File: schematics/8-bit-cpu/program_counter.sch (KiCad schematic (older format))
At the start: 6 parts

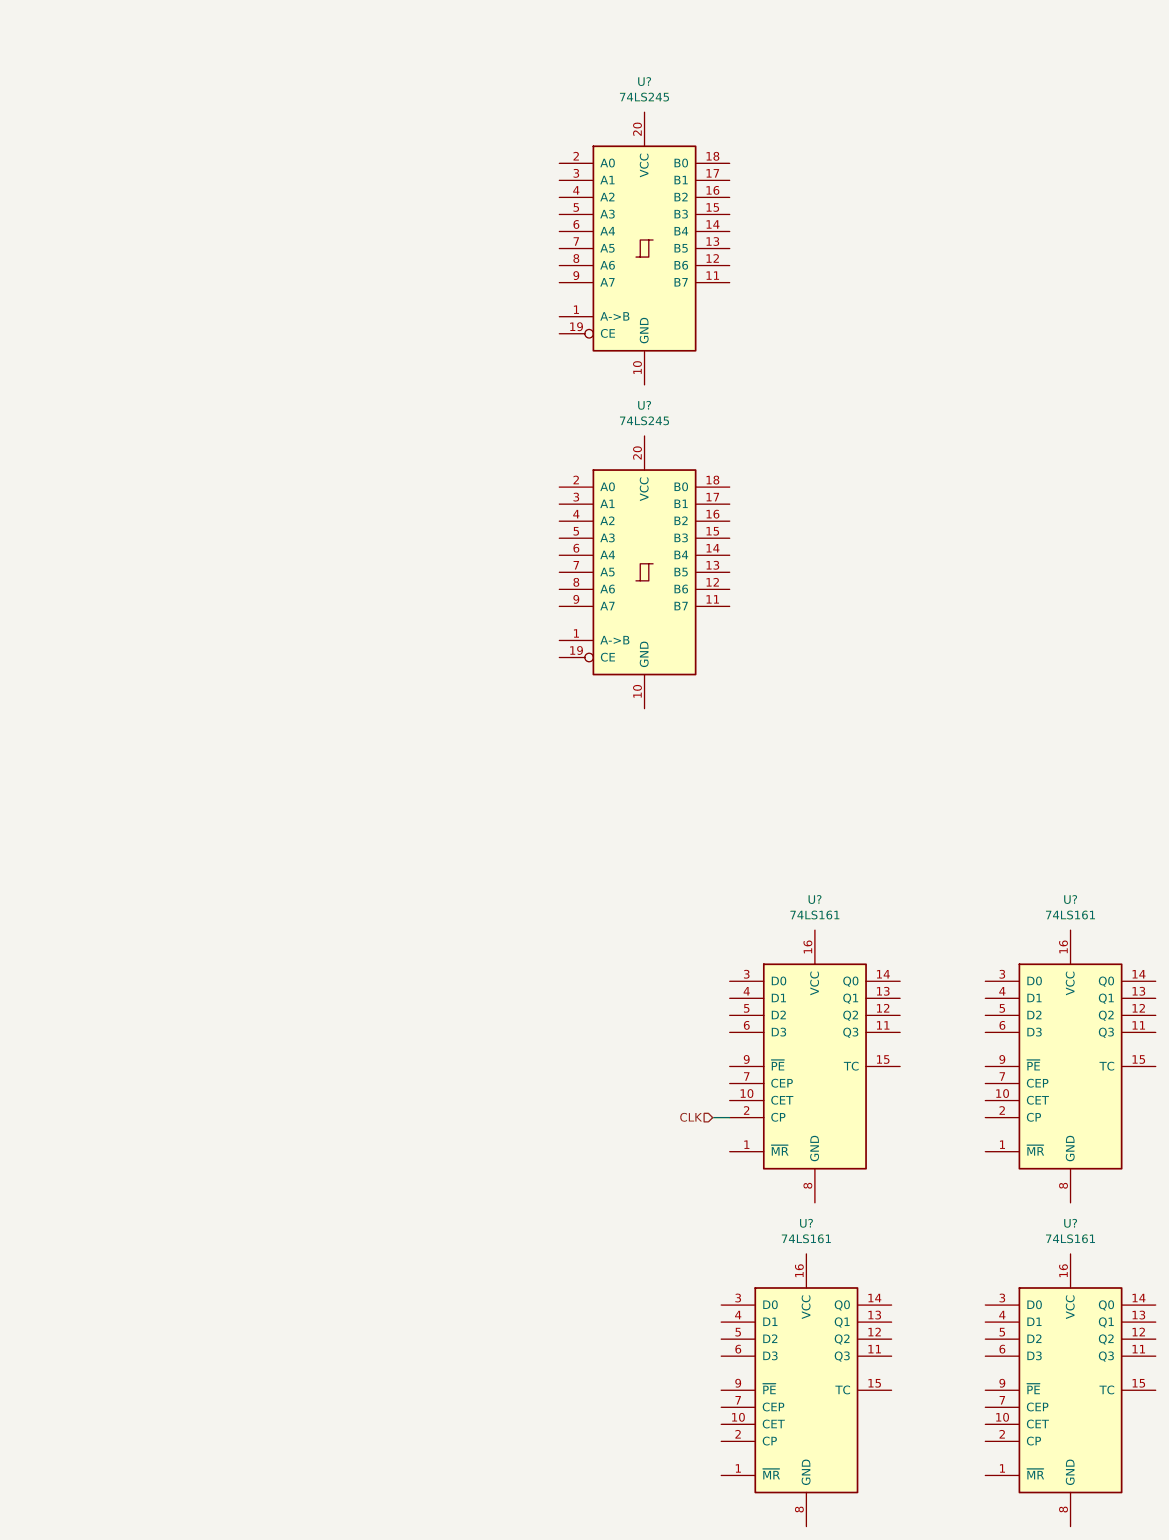
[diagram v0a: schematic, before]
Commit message: Added ALU, Accumulator and HL register schematics
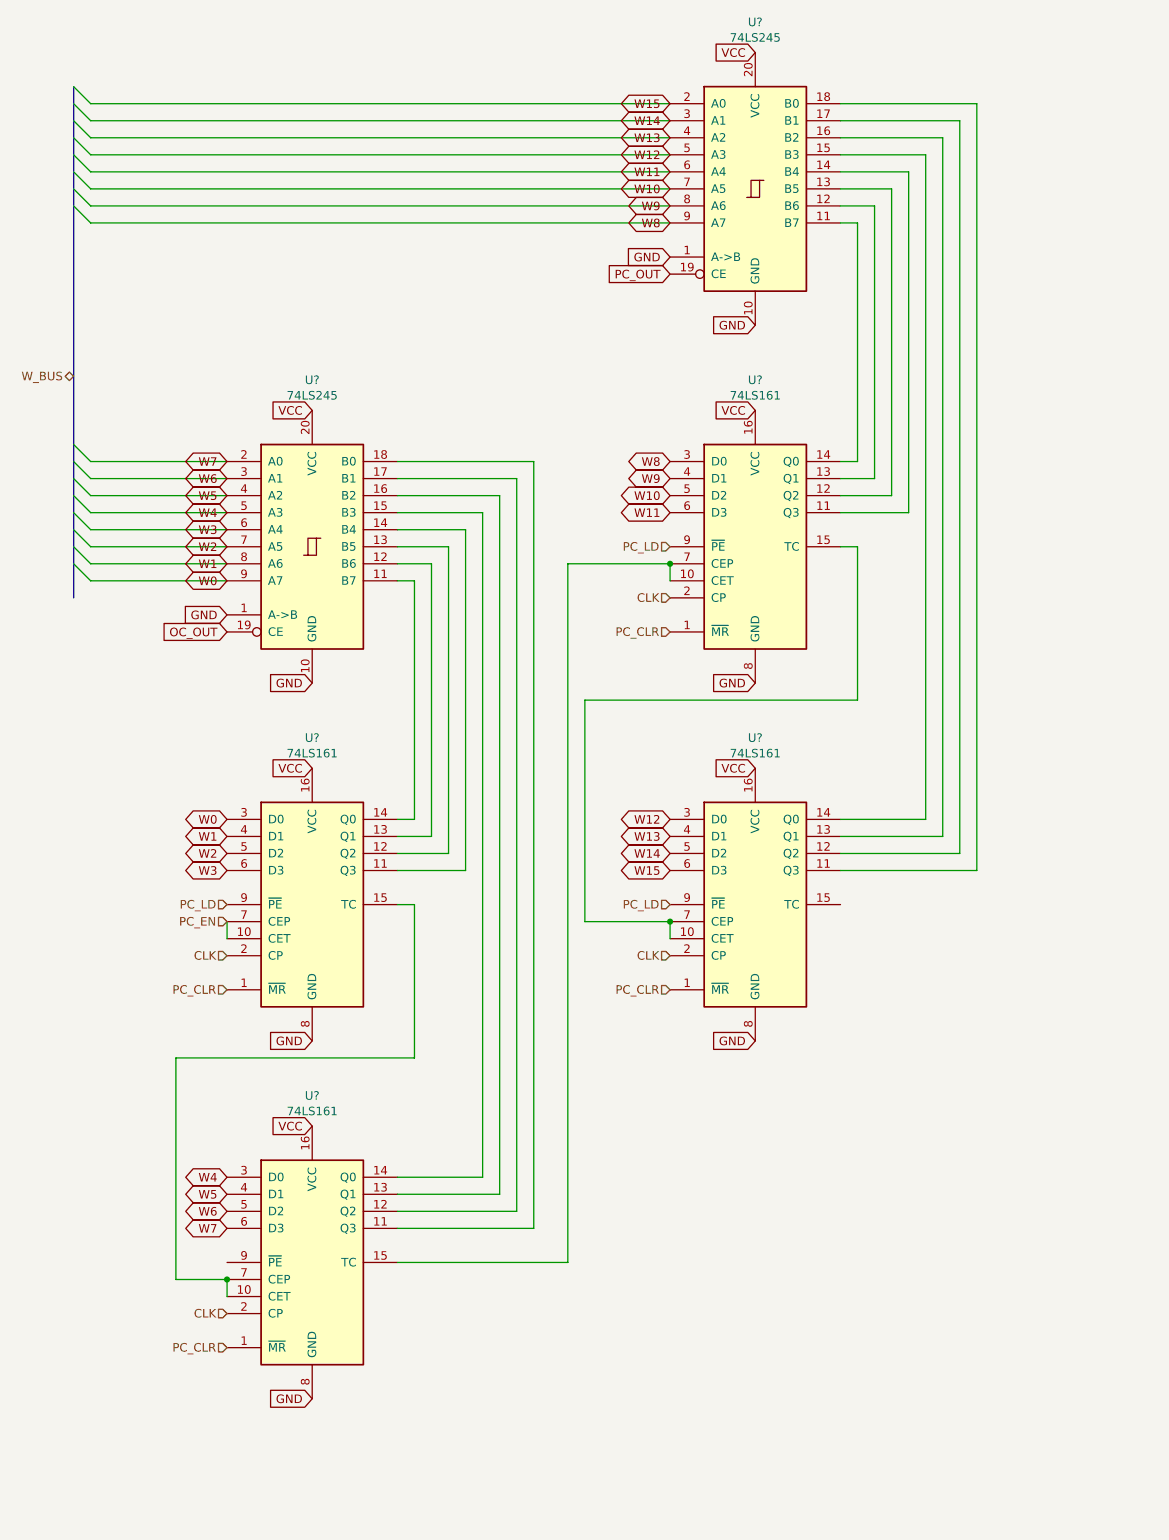
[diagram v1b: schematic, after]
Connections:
- net CLK: now also U?.2 (CP), U?.2 (CP), U?.2 (CP)
- net PC_CLR: now reaches U?.1 (~MR)
- net PC_CLR: now also U?.1 (~MR), U?.1 (~MR), U?.1 (~MR)
- net at U?.10 (CET): now also U?.15 (TC), U?.7 (CEP) (x2)
- net at U?.11 (Q3): now also U?.14 (B4)
- net at U?.12 (Q2): now also U?.13 (B5)
- net at U?.13 (Q1): now also U?.12 (B6)
- net at U?.14 (Q0): now also U?.11 (B7)
- net at U?.15 (TC): now also U?.10 (CET), U?.7 (CEP)
- net VCC: now reaches U?.16 (VCC)
- net VCC: now also U?.16 (VCC), U?.16 (VCC), U?.16 (VCC), U?.20 (VCC), U?.20 (VCC)
- net W8: now reaches U?.3 (D0)
- net W8: now also U?.9 (A7)
- net W9: now reaches U?.4 (D1)
- net W9: now also U?.8 (A6)
- net W10: now reaches U?.5 (D2)
- net W10: now also U?.7 (A5)
- net W11: now reaches U?.6 (D3)
- net W11: now also U?.6 (A4)
- net GND: now reaches U?.8 (GND)
- net GND: now also U?.1 (A->B), U?.1 (A->B), U?.10 (GND), U?.10 (GND), U?.8 (GND), U?.8 (GND), U?.8 (GND)
- net PC_LD: now reaches U?.9 (~PE)
- net PC_LD: now also U?.9 (~PE), U?.9 (~PE)
- net at U?.15 (B3): now also U?.14 (Q0) (x2)
- net at U?.16 (B2): now also U?.13 (Q1) (x2)
- net at U?.17 (B1): now also U?.12 (Q2) (x2)
- net at U?.18 (B0): now also U?.11 (Q3) (x2)
- net PC_OUT: now reaches U?.19 (CE)
- net W15: now reaches U?.2 (A0)
- net W15: now also U?.6 (D3)
- net W14: now reaches U?.3 (A1)
- net W14: now also U?.5 (D2)
- net W13: now reaches U?.4 (A2)
- net W13: now also U?.4 (D1)
- net W12: now reaches U?.5 (A3)
- net W12: now also U?.3 (D0)
- net at U?.11 (B7): now also U?.14 (Q0)
- net at U?.12 (B6): now also U?.13 (Q1)
- net at U?.13 (B5): now also U?.12 (Q2)
- net at U?.14 (B4): now also U?.11 (Q3)
- net OC_OUT: now reaches U?.19 (CE)
- net W7: now reaches U?.2 (A0)
- net W7: now also U?.6 (D3)
- net W6: now reaches U?.3 (A1)
- net W6: now also U?.5 (D2)
- net W5: now reaches U?.4 (A2)
- net W5: now also U?.4 (D1)
- net W4: now reaches U?.5 (A3)
- net W4: now also U?.3 (D0)
- net W3: now reaches U?.6 (A4)
- net W3: now also U?.6 (D3)
- net W2: now reaches U?.7 (A5)
- net W2: now also U?.5 (D2)
- net W1: now reaches U?.8 (A6)
- net W1: now also U?.4 (D1)
- net W0: now reaches U?.9 (A7)
- net W0: now also U?.3 (D0)
- net PC_EN: now reaches U?.10 (CET)
- net PC_EN: now also U?.7 (CEP)
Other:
- moved on the sheet: U?
